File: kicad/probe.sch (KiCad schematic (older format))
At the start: 11 parts

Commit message: Schematic v0.1
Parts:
- removed C? (x2): C, symbol C
- removed D?: D_Schottky, symbol D_Schottky
- removed IC?: ATTINY85-S, SO8-200, symbol ATTINY85-S
- removed R?: R, symbol R
- added 33K1: R, Resistors_SMD:R_0805_HandSoldering, symbol R
- added C1, C3: 10uF, Capacitors_SMD:C_0805_HandSoldering, symbol C
- added C2, C4: 0.1uF, Capacitors_SMD:C_0805_HandSoldering, symbol C
- added D1: Led, theapi_footprints:LED_0805, symbol Led_Small
- added D3: D_Schottky, theapi_footprints:SOD-123-Schottky, symbol D_Schottky
- added IC1: ATTINY85, theapi_footprints:SOIC-8-N-handsolder, symbol ATTINY85-S
- added MOUNT1, MOUNT2, MOUNT3, MOUNT4: CONN_01X01, Pin_Headers:Pin_Header_Straight_1x01, symbol CONN_01X01
- added P1: ICSP, Pin_Headers:Pin_Header_Straight_2x03, symbol CONN_02X03
- added P2: 5V, Pin_Headers:Pin_Header_Straight_1x02, symbol CONN_01X02
- added R1: 10K, Resistors_SMD:R_0805_HandSoldering, symbol R
- added R2: 820, Resistors_SMD:R_0805_HandSoldering, symbol R
- AFF1: renamed from AFF?; footprint (none) -> Displays_7-Segment:Cx56-12
- D2: renamed from D?; footprint (none) -> theapi_footprints:LED_0805
- IC2: renamed from IC?; footprint (none) -> Housings_DIP:DIP-24_W15.24mm
- R3, R4: renamed from R?; footprint (none) -> Resistors_SMD:R_0805_HandSoldering
- TH1: renamed from TH?; footprint (none) -> Discret:R1
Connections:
- net GND: now also C1.2, C2.2, C3.2, C4.2, D1.1 (K), IC1.4 (GND), MOUNT1.1 (P1), MOUNT2.1 (P1), MOUNT3.1 (P1), MOUNT4.1 (P1), P1.6 (P6), P2.1 (P1)
- net VCC: now also R4.1, 33K1.2, C1.1, C2.1, C3.1, C4.1, D3.1 (K), IC1.8 (VCC), P1.2 (P2), R1.2; no longer R4.2
- net at D2.2 (A): now also R4.2; no longer R4.1
- net MOSI: now reaches IC2.1 (DIN)
- net MOSI: now also IC1.5 (PB0(MOSI/DI/SDA/AIN0/OC0A/OC1A/AREF/PCINT0)), P1.4 (P4)
- net PB4: now reaches IC2.12 (LOAD)
- net PB4: now also IC1.3 (PB4(XTAL2/CLKO/OC1B/ADC2/PCINT4))
- net SCK: now reaches IC2.13 (CLK)
- net SCK: now also IC1.7 (PB2(SCK/USCK/SCL/T0/INT0/ADC1/PCINT2)), P1.3 (P3)
- net at IC2.18 (ISET): now also 33K1.1
- net ADC2 renamed ADC3
- net ADC3: now also IC1.2 (PB3(XTAL1/CLKI/OC1B/ADC3/PCINT3))
- new net: D1.2 (A), R2.2
- new net: D3.2 (A), P2.2 (P2)
- new net MISO: IC1.6 (PB1(MISO/DO/AIN1/OC0B/OC1A/PCINT1)), P1.1 (P1), R2.1
- new net RESET: IC1.1 (PB5(~RESET~/dW/ADC0/PCINT5)), P1.5 (P5), R1.1
- no-connect marks 4 -> 5
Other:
- moved on the sheet: AFF1, D2, IC2, R3, R4, TH1

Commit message: Initial layout
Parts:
- IC2: footprint Housings_DIP:DIP-24_W15.24mm -> Housings_DIP:DIP-24_W7.62mm_LongPads
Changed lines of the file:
@@
 F 0 "IC2" H 7900 5200 60  0000 C CNN
 F 1 "MAX7219" H 7900 5200 60  0000 C CNN
-F 2 "Housings_DIP:DIP-24_W15.24mm" H 7900 5200 60  0001 C CNN
+F 2 "Housings_DIP:DIP-24_W7.62mm_LongPads" H 7900 5200 60  0001 C CNN
 F 3 "" H 7900 5200 60  0000 C CNN
 	1    7900 5200

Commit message: New layout with correct size display
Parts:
- AFF1: footprint Displays_7-Segment:Cx56-12 -> theapi_footprints:4x7seg_CA
- IC2: footprint Housings_DIP:DIP-24_W7.62mm_LongPads -> Housings_DIP:DIP-24_W7.62mm
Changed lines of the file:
@@
 F 0 "IC2" H 7900 5200 60  0000 C CNN
 F 1 "MAX7219" H 7900 5200 60  0000 C CNN
-F 2 "Housings_DIP:DIP-24_W7.62mm_LongPads" H 7900 5200 60  0001 C CNN
+F 2 "Housings_DIP:DIP-24_W7.62mm" H 7900 5200 60  0001 C CNN
 F 3 "" H 7900 5200 60  0000 C CNN
 	1    7900 5200
@@
 F 0 "AFF1" H 9350 3050 50  0000 C CNN
 F 1 "CC56-12" H 9350 2950 50  0000 C CNN
-F 2 "Displays_7-Segment:Cx56-12" H 8850 2300 50  0001 C CNN
+F 2 "theapi_footprints:4x7seg_CA" H 8850 2300 50  0001 C CNN
 F 3 "" H 8850 2300 50  0000 C CNN
 	1    9350 2300

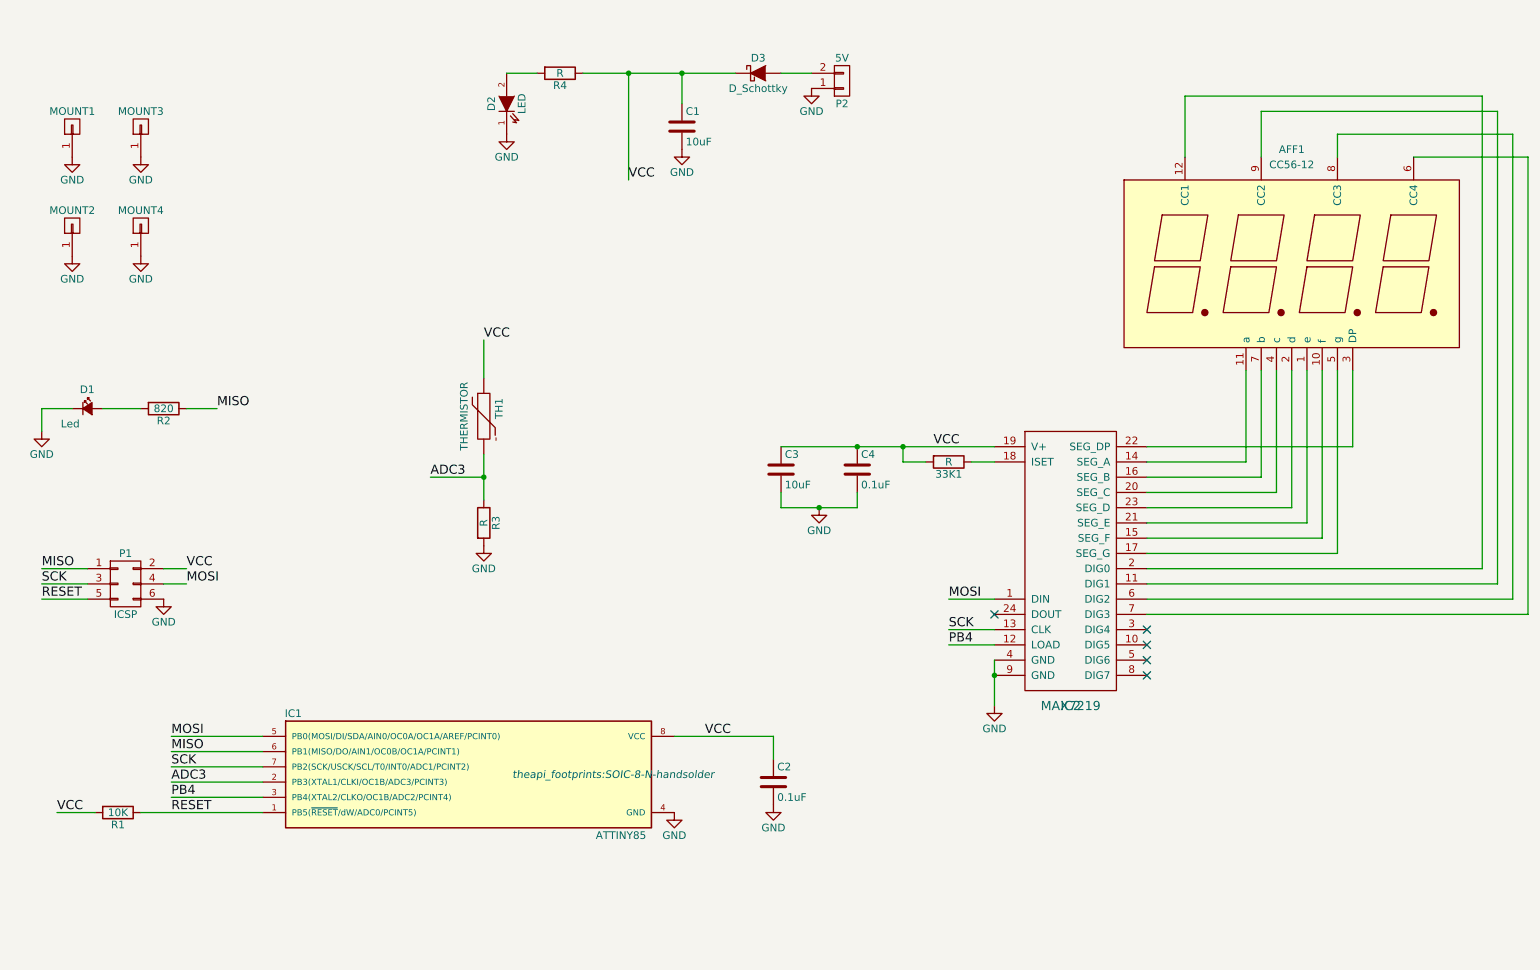
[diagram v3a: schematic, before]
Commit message: 2 displays & 2 thermistors on perfboard
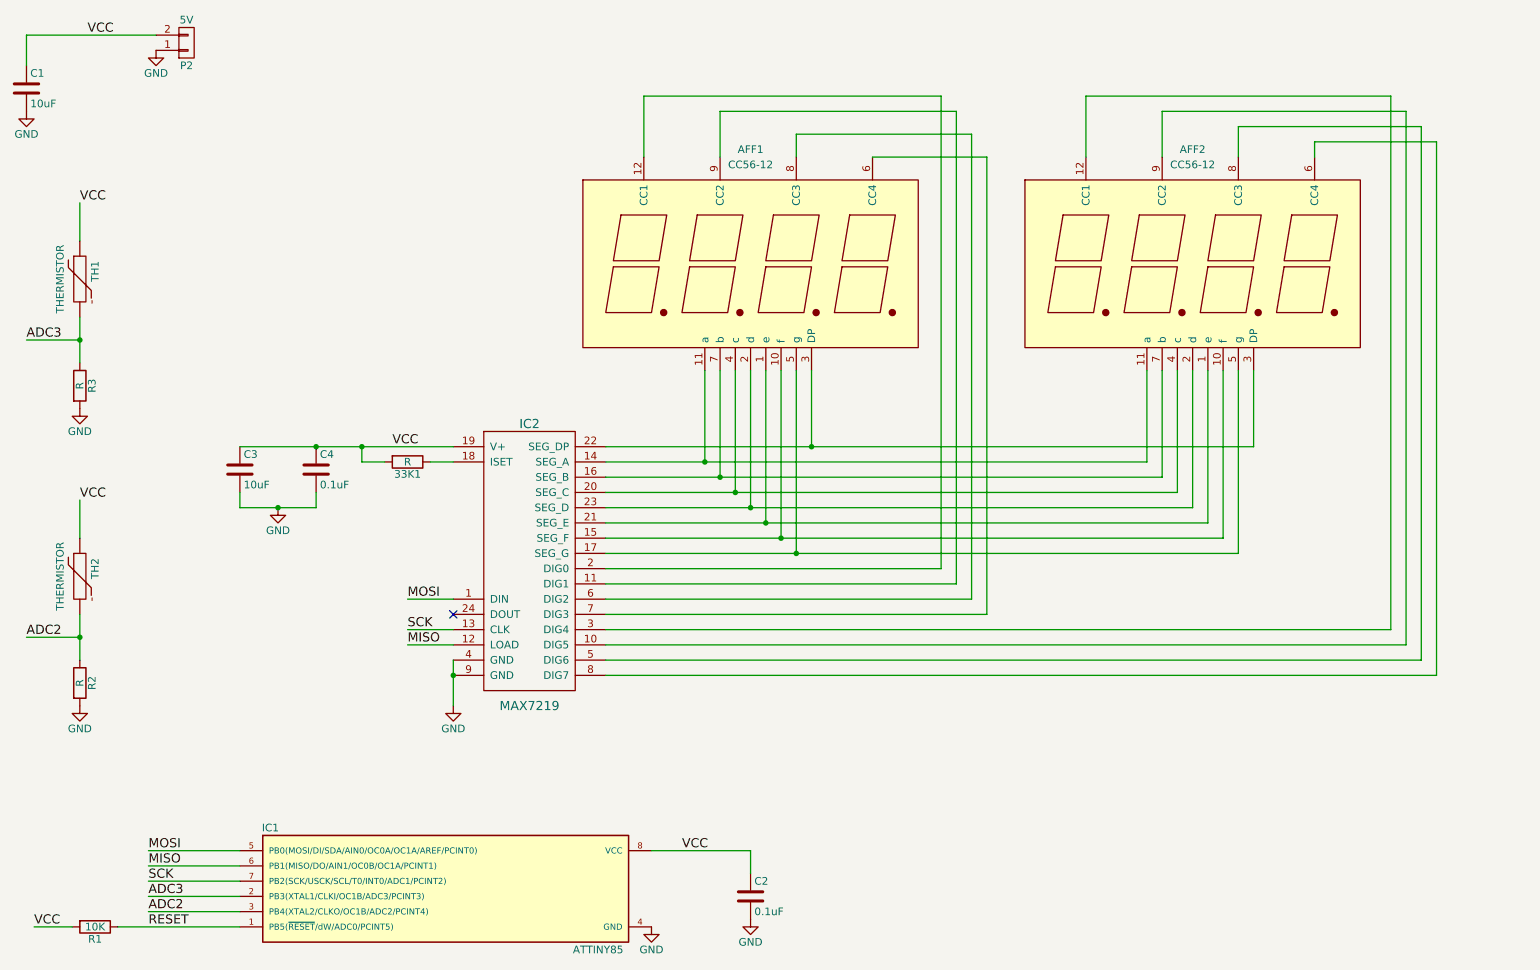
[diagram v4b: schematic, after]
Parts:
- removed D1: Led, theapi_footprints:LED_0805, symbol Led_Small
- removed D2: LED, theapi_footprints:LED_0805, symbol LED
- removed D3: D_Schottky, theapi_footprints:SOD-123-Schottky, symbol D_Schottky
- removed MOUNT1, MOUNT2, MOUNT3, MOUNT4: CONN_01X01, Pin_Headers:Pin_Header_Straight_1x01, symbol CONN_01X01
- removed P1: ICSP, Pin_Headers:Pin_Header_Straight_2x03, symbol CONN_02X03
- removed R4: R, Resistors_SMD:R_0805_HandSoldering, symbol R
- added AFF2: CC56-12, theapi_footprints:4x7seg_CA, symbol CC56-12
- added TH2: THERMISTOR, Discret:R1, symbol THERMISTOR
- IC1: footprint theapi_footprints:SOIC-8-N-handsolder -> Housings_DIP:DIP-8_W7.62mm
- R2: value 820 -> R
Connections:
- net GND: now also R2.2
- net MISO: now also IC2.12 (LOAD); no longer R2.1
- net VCC: now also P2.2 (P2), TH2.1
- net at IC2.10 (DIG5): now also AFF2.9 (CC2)
- net at AFF1.11 (a), IC2.14 (SEG_A): now also AFF2.11 (a)
- net at AFF1.10 (f), IC2.15 (SEG_F): now also AFF2.10 (f)
- net at AFF1.7 (b), IC2.16 (SEG_B): now also AFF2.7 (b)
- net at AFF1.5 (g), IC2.17 (SEG_G): now also AFF2.5 (g)
- net at AFF1.4 (c), IC2.20 (SEG_C): now also AFF2.4 (c)
- net at AFF1.1 (e), IC2.21 (SEG_E): now also AFF2.1 (e)
- net at AFF1.3 (DP), IC2.22 (SEG_DP): now also AFF2.3 (DP)
- net at AFF1.2 (d), IC2.23 (SEG_D): now also AFF2.2 (d)
- net at IC2.3 (DIG4): now also AFF2.12 (CC1)
- net at IC2.5 (DIG6): now also AFF2.8 (CC3)
- net at IC2.8 (DIG7): now also AFF2.6 (CC4)
- net PB4 renamed ADC2
- net ADC2: now also R2.1, TH2.2; no longer IC2.12 (LOAD)
- no-connect marks 5 -> 1
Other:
- moved on the sheet: 33K1, AFF1, C1, C2, C3, C4, IC1, IC2, P2, R1, R3, TH1

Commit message: Better accuracy
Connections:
- net ADC2: now also R2.2, TH2.1; no longer R2.1, TH2.2
- net ADC3: now also R3.2, TH1.1; no longer R3.1, TH1.2
- net GND: now also TH1.2, TH2.2; no longer R2.2, R3.2
- net VCC: now also R2.1, R3.1; no longer TH1.1, TH2.1
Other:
- moved on the sheet: R2, R3, TH1, TH2
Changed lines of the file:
@@
 L THERMISTOR TH1
 U 1 1 57D69809
-P 1400 2400
-F 0 "TH1" V 1500 2450 50  0000 C CNN
-F 1 "THERMISTOR" V 1300 2400 50  0000 C BNN
-F 2 "Discret:R1" H 1400 2400 50  0001 C CNN
-F 3 "" H 1400 2400 50  0000 C CNN
-	1    1400 2400
+P 1400 3200
+F 0 "TH1" V 1500 3250 50  0000 C CNN
+F 1 "THERMISTOR" V 1300 3200 50  0000 C BNN
+F 2 "Discret:R1" H 1400 3200 50  0001 C CNN
+F 3 "" H 1400 3200 50  0000 C CNN
+	1    1400 3200
 	1    0    0    -1
 $EndComp
@@
 L R R3
 U 1 1 57D698E5
-P 1400 3100
-F 0 "R3" V 1480 3100 50  0000 C CNN
-F 1 "R" V 1400 3100 50  0000 C CNN
-F 2 "Resistors_SMD:R_0805_HandSoldering" V 1330 3100 50  0001 C CNN
-F 3 "" H 1400 3100 50  0000 C CNN
-	1    1400 3100
+P 1400 2500
+F 0 "R3" V 1480 2500 50  0000 C CNN
+F 1 "R" V 1400 2500 50  0000 C CNN
+F 2 "Resistors_SMD:R_0805_HandSoldering" V 1330 2500 50  0001 C CNN
+F 3 "" H 1400 2500 50  0000 C CNN
+	1    1400 2500
 	1    0    0    -1
 $EndComp
@@
 L GND #PWR2
 U 1 1 57D6D625
-P 1400 3250
-F 0 "#PWR2" H 1400 3000 50  0001 C CNN
-F 1 "GND" H 1400 3100 50  0000 C CNN
-F 2 "" H 1400 3250 50  0000 C CNN
-F 3 "" H 1400 3250 50  0000 C CNN
-	1    1400 3250
+P 1400 3450
+F 0 "#PWR2" H 1400 3200 50  0001 C CNN
+F 1 "GND" H 1400 3300 50  0000 C CNN
+F 2 "" H 1400 3450 50  0000 C CNN
+F 3 "" H 1400 3450 50  0000 C CNN
+	1    1400 3450
 	1    0    0    -1
 $EndComp
@@
 Wire Wire Line
 	1050 2800 1400 2800
-Text Label 1400 1900 0    60   ~ 0
-VCC
-Wire Wire Line
-	1400 1900 1400 2150
+Text Label 1400 2100 0    60   ~ 0
+VCC
+Wire Wire Line
+	1400 2100 1400 2350
 Text Label 3450 3500 0    60   ~ 0
 VCC
@@
 L THERMISTOR TH2
 U 1 1 57DEB3C1
-P 1400 4350
-F 0 "TH2" V 1500 4400 50  0000 C CNN
-F 1 "THERMISTOR" V 1300 4350 50  0000 C BNN
-F 2 "Discret:R1" H 1400 4350 50  0001 C CNN
-F 3 "" H 1400 4350 50  0000 C CNN
-	1    1400 4350
+P 1400 5150
+F 0 "TH2" V 1500 5200 50  0000 C CNN
+F 1 "THERMISTOR" V 1300 5150 50  0000 C BNN
+F 2 "Discret:R1" H 1400 5150 50  0001 C CNN
+F 3 "" H 1400 5150 50  0000 C CNN
+	1    1400 5150
 	1    0    0    -1
 $EndComp
@@
 L R R2
 U 1 1 57DEB3C7
-P 1400 5050
-F 0 "R2" V 1480 5050 50  0000 C CNN
-F 1 "R" V 1400 5050 50  0000 C CNN
-F 2 "Resistors_SMD:R_0805_HandSoldering" V 1330 5050 50  0001 C CNN
-F 3 "" H 1400 5050 50  0000 C CNN
-	1    1400 5050
+P 1400 4450
+F 0 "R2" V 1480 4450 50  0000 C CNN
+F 1 "R" V 1400 4450 50  0000 C CNN
+F 2 "Resistors_SMD:R_0805_HandSoldering" V 1330 4450 50  0001 C CNN
+F 3 "" H 1400 4450 50  0000 C CNN
+	1    1400 4450
 	1    0    0    -1
 $EndComp
@@
 L GND #PWR3
 U 1 1 57DEB3CD
-P 1400 5200
-F 0 "#PWR3" H 1400 4950 50  0001 C CNN
-F 1 "GND" H 1400 5050 50  0000 C CNN
-F 2 "" H 1400 5200 50  0000 C CNN
-F 3 "" H 1400 5200 50  0000 C CNN
-	1    1400 5200
+P 1400 5400
+F 0 "#PWR3" H 1400 5150 50  0001 C CNN
+F 1 "GND" H 1400 5250 50  0000 C CNN
+F 2 "" H 1400 5400 50  0000 C CNN
+F 3 "" H 1400 5400 50  0000 C CNN
+	1    1400 5400
 	1    0    0    -1
 $EndComp
@@
 Wire Wire Line
 	1050 4750 1400 4750
-Text Label 1400 3850 0    60   ~ 0
-VCC
-Wire Wire Line
-	1400 3850 1400 4100
+Text Label 1400 4050 0    60   ~ 0
+VCC
+Wire Wire Line
+	1400 4050 1400 4300
 Text Label 3550 4800 0    60   ~ 0
 MISO
